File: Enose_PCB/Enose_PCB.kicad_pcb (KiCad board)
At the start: 2 copper layers, 120 x 100 mm, 147 parts, among them IC1 ISL91127IRNZ-T7A, IC2 MP2722GRH-0000-Z, IC3 TPS22958DGNR, J1 Conn_01x04_Pin, J10 Fan, J2 Conn_01x04_Pin, J3 Conn_01x04_Pin, J4 DA15_Pins, J5 USB_C_Receptacle_USB2.0_16P, J6 Battery Terminal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

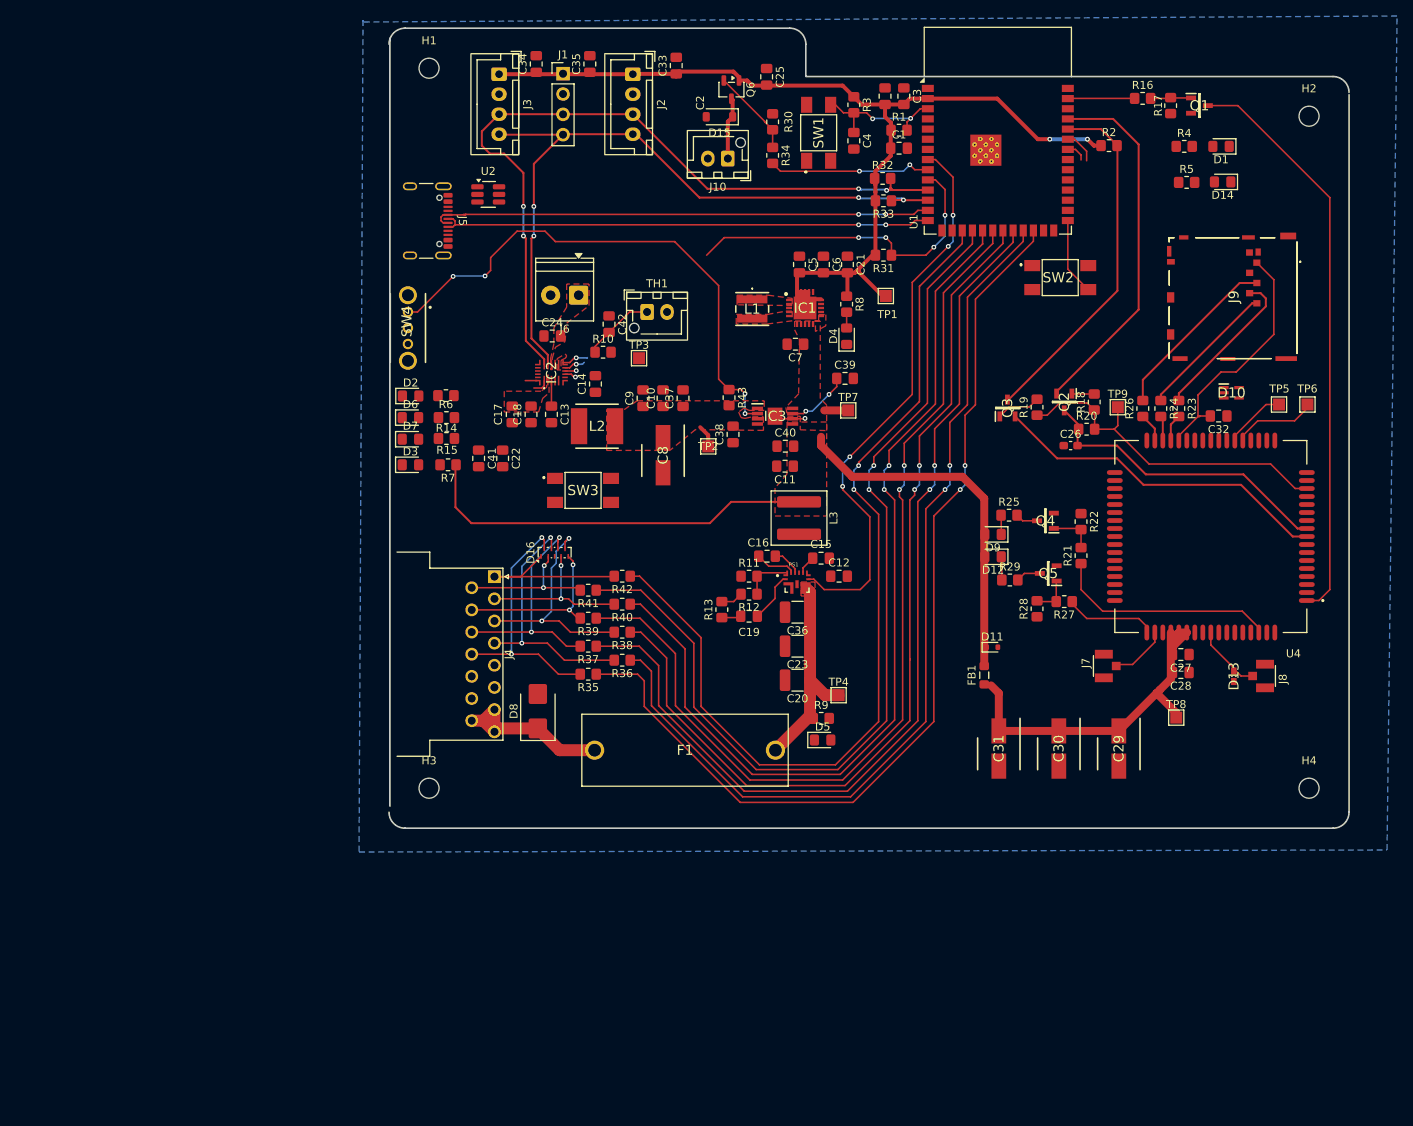
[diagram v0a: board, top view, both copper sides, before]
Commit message: Enose PCB almost done, just needs ground vias
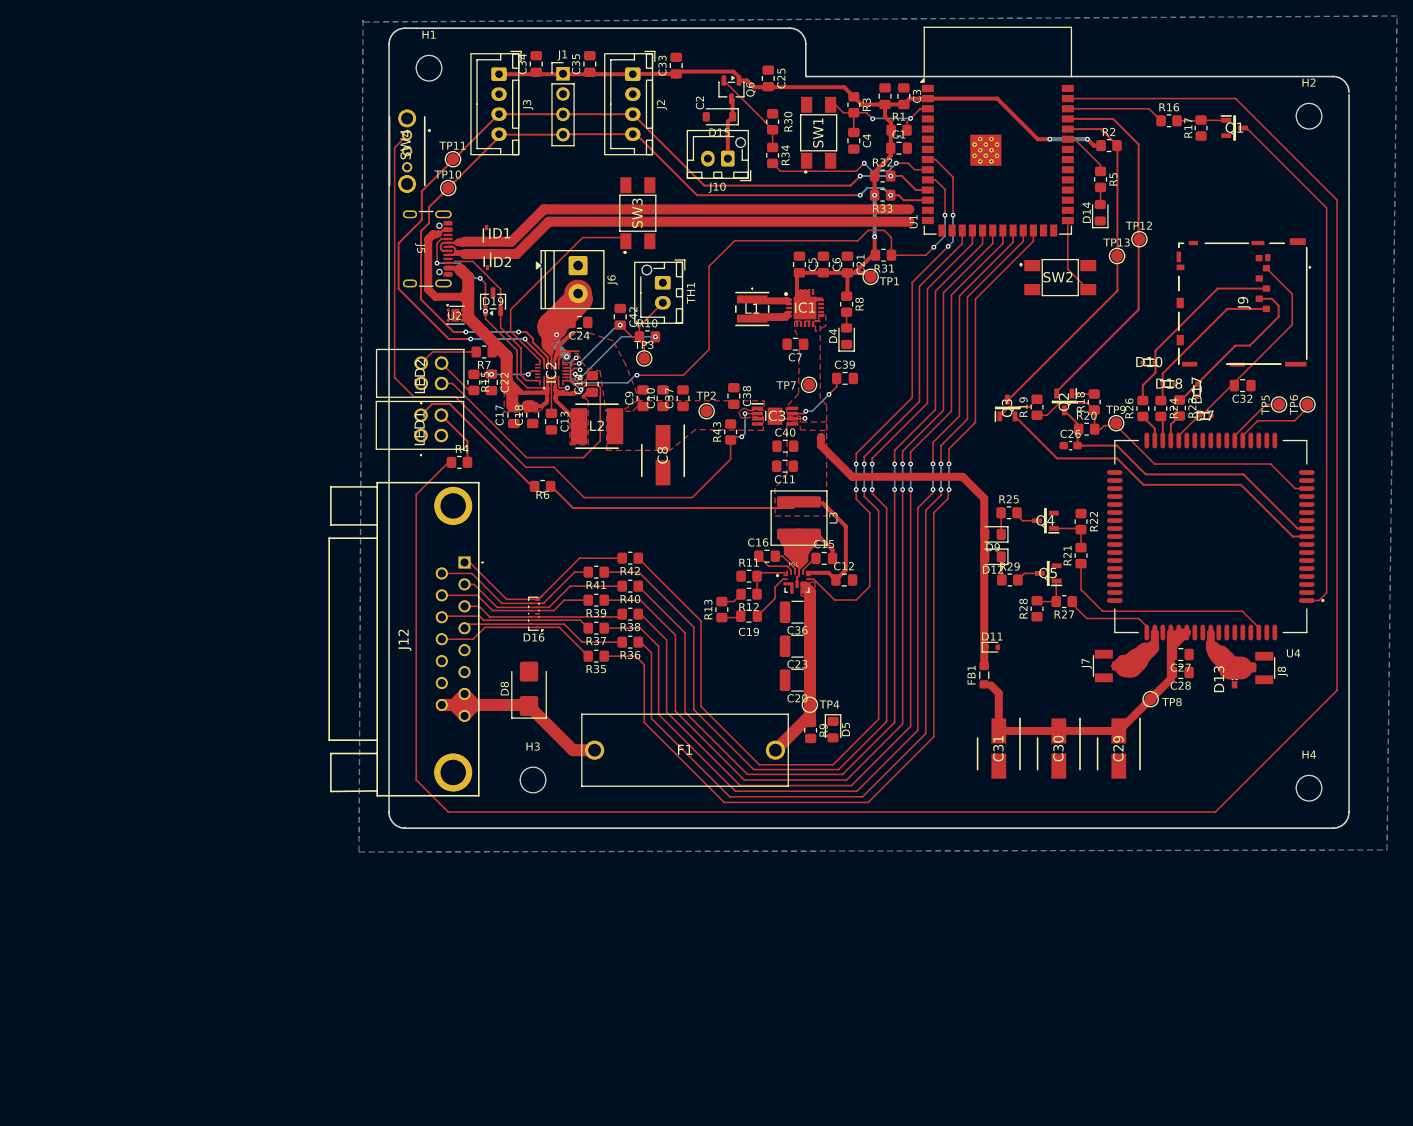
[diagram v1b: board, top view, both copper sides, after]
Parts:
- removed C41: 2.2uF, Capacitor_SMD:C_0805_2012Metric_Pad1.18x1.45mm_HandSolder
- removed D3: LED, LED_SMD:LED_0805_2012Metric_Pad1.15x1.40mm_HandSolder
- removed D6: Amber LED, LED_SMD:LED_0805_2012Metric_Pad1.15x1.40mm_HandSolder
- removed J4: DA15_Pins, Connector_Dsub:DSUB-15_Pins_Horizontal_P2.77x2.84mm_EdgePinOffset9.40mm
- removed R14: 510, Resistor_SMD:R_0805_2012Metric_Pad1.20x1.40mm_HandSolder
- added D17: ESD8351XV2T1G, SamacSys_Parts:SODFL1608X70N, F.Cu at (176.0, 95.3)
- added D18: ESD8351XV2T1G, SamacSys_Parts:SODFL1608X70N, F.Cu at (172.5, 94.5)
- added D19: ESDS452DBZR, Package_TO_SOT_SMD:SOT-23-3, F.Cu at (88.0, 84.2)
- added J12: DA15_Pins_MountingHoles, SamacSys_Parts:6E17C015PAJ121, F.Cu at (84.4, 116.8)
- added LED1: 552-0212F, SamacSys_Parts:5520212F, F.Cu at (79.0, 100.9)
- added LED2: 552-0212F, SamacSys_Parts:5520212F, F.Cu at (79.0, 94.4)
- added TP10: TestPoint, TestPoint:TestPoint_Pad_D1.5mm, F.Cu at (82.4, 70.0)
- added TP11: TestPoint, TestPoint:TestPoint_Pad_D1.5mm, F.Cu at (83.0, 66.4)
- added TP12: TestPoint, TestPoint:TestPoint_Pad_D1.5mm, F.Cu at (168.8, 76.4)
- added TP13: TestPoint, TestPoint:TestPoint_Pad_D1.5mm, F.Cu at (166.0, 78.5)
- D1: value LED Amber -> ESD8351XV2T1G; footprint LED_SMD:LED_0805_2012Metric_Pad1.15x1.40mm_HandSolder -> SamacSys_Parts:SODFL1608X70N
- D10: value ESDALC6V1W5 -> ESD8351XV2T1G; footprint ESDALC6V1W5:SOT65P210X110-5N -> SamacSys_Parts:SODFL1608X70N
- D2: value LED -> ESD8351XV2T1G; footprint LED_SMD:LED_0805_2012Metric_Pad1.15x1.40mm_HandSolder -> SamacSys_Parts:SODFL1608X70N
- D7: value Amber LED -> ESD8351XV2T1G; footprint LED_SMD:LED_0805_2012Metric_Pad1.15x1.40mm_HandSolder -> SamacSys_Parts:SODFL1608X70N
- H1, H2, H3, H4: footprint MountingHole:MountingHole_2.5mm -> MountingHole:MountingHole_3.2mm_M3
- R6: value 1k -> 680
- R7: value 680 -> 1k
- TP1, TP2, TP3, TP4, TP5, TP6, TP7, TP8, TP9: footprint TestPoint:TestPoint_Pad_1.5x1.5mm -> TestPoint:TestPoint_Pad_D1.5mm
- U2: value USBLC6-4SC6 -> TVS0500DRV; footprint Package_TO_SOT_SMD:SOT-23-6_Handsoldering -> Package_SON:WSON-6-1EP_2x2mm_P0.65mm_EP1x1.6mm
- moved D7 99.4 mm to (177.0, 98.5)
- moved R4 98.8 mm to (83.8, 104.3)
- moved D1 92.4 mm to (87.2, 75.7), turned to 90 degrees
- moved SW3 35.3 mm to (106.1, 73.2), turned to 90 degrees
- moved SW4 22.1 mm to (77.3, 65.4)
- moved D2 19.3 mm to (87.3, 79.2), turned to -90 degrees
- moved R6 16.6 mm to (94.2, 107.3)
- moved D14 15.8 mm to (163.9, 73.1), turned to 90 degrees
- moved U2 15.6 mm to (83.3, 85.9)
- moved R7 14.8 mm to (86.9, 90.5)
- moved H3 13.0 mm to (93.0, 144.0)
- moved D10 11.0 mm to (170.0, 91.8), turned to 180 degrees
- moved R5 10.8 mm to (163.9, 68.9), turned to -90 degrees
- moved C22 9.60 mm to (87.8, 94.3)
- moved D16 8.08 mm to (93.1, 123.2), turned to 180 degrees
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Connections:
- net /ESP_LED2 renamed Net-(U1-IO42)
- net Net-(IC2-SW) renamed /Power Components/SW_Inductor_IN
- D1 pad 1: GND -> USB_D-
- D1 pad 2: Net-(D1-A) -> GND
- D10 pad 1: Net-(J9-I/O) -> Net-(D10-K)
- D2 pad 1: GND -> USB_D+
- D2 pad 2: Net-(D2-A) -> GND
- D7 pad 1: /Power Components/STAT/IB -> /Cellular Module/SIM_VDD
- D7 pad 2: Net-(D7-A) -> GND
- J6 pad 1: +BATT -> GND
- J6 pad 2: GND -> +BATT
- J9 pad 2: Net-(J9-RST) -> Net-(D10-K)
- J9 pad 3: Net-(J9-CLK) -> Net-(D18-K)
- J9 pad 6: Net-(J9-I/O) -> Net-(D17-K)
- R15 pad 2: Net-(D7-A) -> Net-(LED2-ANODE_2)
- R23 pad 1: Net-(J9-I/O) -> Net-(D17-K)
- R24 pad 1: Net-(J9-CLK) -> Net-(D18-K)
- R26 pad 2: Net-(J9-RST) -> Net-(D10-K)
- R35 pad 1: /PWM8 -> /PWM1
- R35 pad 2: Net-(D16-K8) -> Net-(D16-K1)
- R36 pad 1: /PWM7 -> /PWM2
- R36 pad 2: Net-(D16-K7) -> Net-(D16-K8)
- R37 pad 1: /PWM6 -> /PWM3
- R37 pad 2: Net-(D16-K6) -> Net-(D16-K2)
- R38 pad 1: /PWM5 -> /PWM4
- R38 pad 2: Net-(D16-K5) -> Net-(D16-K7)
- R39 pad 1: /PWM4 -> /PWM5
- R39 pad 2: Net-(D16-K4) -> Net-(D16-K6)
- R4 pad 1: /ESP_LED1 -> /POWER_STATUS
- R4 pad 2: Net-(D1-A) -> Net-(LED1-ANODE_2)
- R40 pad 1: /PWM3 -> /PWM6
- R41 pad 1: /PWM2 -> /PWM7
- R41 pad 2: Net-(D16-K2) -> Net-(D16-K5)
- R42 pad 1: /PWM1 -> /PWM8
- R42 pad 2: Net-(D16-K1) -> Net-(D16-K4)
- R6 pad 1: VBUS -> +SYS_SW
- R6 pad 2: Net-(D2-A) -> Net-(LED1-ANODE_1)
- R7 pad 1: +SYS_SW -> +VBUS
- TH1 pad 1: /Power Components/NTC1 -> GND
- TH1 pad 2: GND -> /Power Components/NTC1
- U1 pad 17: /PWM1 -> /PWM8
- U1 pad 18: /PWM2 -> /PWM7
- U1 pad 19: /PWM3 -> /PWM6
- U1 pad 20: /PWM4 -> /PWM5
- U1 pad 21: /PWM5 -> /PWM4
- U1 pad 22: /PWM6 -> /PWM3
- U1 pad 23: /PWM7 -> /PWM2
- U1 pad 24: /PWM8 -> /PWM1
- U1 pad 34: /ESP_LED1 -> unconnected-(U1-IO41-Pad34)
- U1 pad 38: unconnected-(U1-IO2-Pad38) -> PWRKEY
- U1 pad 39: PWRKEY -> /POWER_STATUS
- U2 pad 1: /Power Components/CC1 -> GND
- U2 pad 3: /Power Components/CC2 -> GND
- U2 pad 4: USB_D- -> +VBUS
- U2 pad 6: USB_D+ -> +VBUS
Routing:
- net /POWER_STATUS: track 0.00 -> 265.0 mm
- net +VBUS: track 0.00 -> 56.3 mm
- net /Power Components/STAT/IB: track 3.44 -> 40.8 mm, vias 1 -> 2
- net +BATT: track 0.00 -> 31.9 mm, vias 0 -> 2
- net ~{INT}: track 43.4 -> 74.4 mm, vias 5 -> 4
- net Net-(C15-Pad1): track 0.00 -> 27.4 mm
- net /Power Components/CC1: track 2.05 -> 29.4 mm, vias 0 -> 3
- net /Power Components/~{RST}: track 0.00 -> 26.3 mm
- net Net-(D10-K): track 0.00 -> 24.7 mm
- net Net-(IC3-ON): track 66.6 -> 89.7 mm, vias 4 -> 2
- net Net-(J9-RST): track 21.9 -> 0.00 mm
- net Net-(D17-K): track 0.00 -> 20.9 mm
- net /Cellular Module/GNSS_ANT: track 7.07 -> 27.9 mm
- net /Power Components/CC2: track 1.47 -> 22.2 mm
- net Net-(D18-K): track 0.00 -> 19.9 mm
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- added copper zone on F.Cu, net /Power Components/SW_Inductor_IN
- removed copper zone on F.Cu, net +BATT
- removed copper zone on F.Cu, net /Power Components/LX1
- removed copper zone on F.Cu, net /Power Components/LX2
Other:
- outline, holes or cut-outs redrawn

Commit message: Enose board ready for review
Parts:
- added H5: MountingHole, MountingHole:MountingHole_3.2mm_M3, F.Cu at (53.7, 146.4)
- added J4: Conn_01x05_Pin, Connector_PinHeader_2.54mm:PinHeader_1x05_P2.54mm_Vertical, F.Cu at (126.2, 102.3)
- added TP14: TestPoint, TestPoint:TestPoint_Pad_D1.5mm, F.Cu at (133.6, 117.7)
- added TP15: TestPoint, TestPoint:TestPoint_Pad_D1.5mm, F.Cu at (97.3, 121.4)
- added TP16: TestPoint, TestPoint:TestPoint_Pad_D1.5mm, F.Cu at (115.9, 165.1)
- moved D14 70.3 mm to (113.1, 121.7)
- moved R5 70.3 mm to (113.2, 117.5)
- moved TP3 66.4 mm to (51.2, 127.4)
- moved C32 53.2 mm to (141.2, 129.2), turned to -90 degrees
- moved SW2 53.1 mm to (118.2, 115.3), turned to 90 degrees
- moved TP6 52.1 mm to (150.0, 130.8)
- moved R10 52.1 mm to (67.2, 121.8), turned to -90 degrees
- moved TP11 51.5 mm to (43.4, 99.4)
- moved C42 51.3 mm to (65.0, 119.5)
- moved Q1 51.0 mm to (143.2, 97.0)
- moved R16 51.0 mm to (135.1, 96.2)
- moved R17 51.0 mm to (139.1, 97.0)
- moved C36 50.9 mm to (87.0, 155.8)
- moved TP10 50.9 mm to (43.2, 102.4)
- moved H3 50.8 mm to (53.7, 176.2)
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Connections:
- R5 pad 1: Net-(U1-IO42) -> Net-(U1-IO38)
- TP3 pad 1: /Power Components/NTC1 -> +VBUS
- U1 pad 31: unconnected-(U1-IO38-Pad31) -> Net-(U1-IO38)
- U1 pad 33: unconnected-(U1-IO40-Pad33) -> Net-(J4-Pin_5)
- U1 pad 34: unconnected-(U1-IO41-Pad34) -> Net-(J4-Pin_4)
- U1 pad 35: Net-(U1-IO42) -> Net-(J4-Pin_3)
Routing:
- net Net-(U1-IO38): track 0.00 -> 22.6 mm
- net Net-(J4-Pin_5): track 0.00 -> 16.5 mm
- net Net-(J4-Pin_4): track 0.00 -> 15.2 mm
- net Net-(J4-Pin_3): track 0.00 -> 14.0 mm
- net +15V: track 22.1 -> 32.3 mm
- net GND: track 11.8 -> 20.1 mm, vias 2 -> 422
- net USB_D+: track 64.3 -> 71.8 mm
- net Net-(U1-IO42): track 6.21 -> 0.00 mm
- net +3V3: track 132.8 -> 138.2 mm
- net ~{INT}: track 74.4 -> 69.2 mm
- net USB_D-: track 65.3 -> 69.5 mm
- net /Power Components/NTC1: track 20.5 -> 16.9 mm
- net Net-(SW2-B): track 9.69 -> 6.46 mm
- net Net-(D5-A): track 0.00 -> 2.91 mm
- net Net-(D17-K): track 20.9 -> 23.7 mm
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- added copper zone on F.Cu, net GND
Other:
- outline, holes or cut-outs redrawn
- board text added: "15V"
- board text added: "3V3"
- board text added: "GND"
- board text added: "GPIO40"
- board text added: "GPIO41"
- board text added: "GPIO42"
- board text added: "NTC"
- board text added: "RX"
- board text added: "RXD"
- board text added: "SCL"
- board text added: "SDA"
- board text added: "SYS"
- board text added: "SYS_SW"
- board text added: "TX"
- board text added: "TXD"
- board text added: "VBAT"
- board text added: "VBUS"
- board text added: "VDD_EXT"
- board text added: "VFAN"
- board text added: "Vin"

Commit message: Enose PCB finished
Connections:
- IC2 pad 9: /Power Components/PG/NTC2 -> unconnected-(IC2-PG/_NTC2-Pad9)
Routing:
- net +BATT: track 31.9 -> 27.6 mm
- net I2C_SDA: track 109.0 -> 109.5 mm
- net GND: vias 422 -> 421
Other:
- board text added: "BOOT"
- board text added: "MP2722 RESTART"
- board text added: "RESTART"
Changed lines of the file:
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@@
 	(net 18 "Net-(D4-A)")
 	(net 19 "Net-(D5-A)")
-	(net 20 "/Power Components/PG{slash}NTC2")
+	(net 20 "unconnected-(IC2-PG{slash}_NTC2-Pad9)")
 	(net 21 "/POWER_STATUS")
 	(net 22 "/Power Components/STAT{slash}IB")
@@
 		(tags "Integrated Circuit")
 		(property "Reference" "IC2"
-			(at 3.525 0.15 180)
+			(at 3.525 -0.05 180)
 			(layer "F.SilkS")
 			(effects
@@
 			(size 0.2 0.7)
 			(layers "F.Cu" "F.Mask" "F.Paste")
-			(net 20 "/Power Components/PG{slash}NTC2")
+			(net 20 "unconnected-(IC2-PG{slash}_NTC2-Pad9)")
 			(pinfunction "PG/_NTC2")
-			(pintype "passive")
+			(pintype "passive+no_connect")
 		)
 		(pad "10" smd rect
@@
 			(at 0.05 3.95 270)
 			(layer "F.SilkS")
+			(hide yes)
 			(effects
 				(font
@@
 			(at -6.75 0.05 180)
 			(layer "F.SilkS")
+			(hide yes)
 			(effects
 				(font
@@
 			(at 0 4.95 180)
 			(layer "F.SilkS")
+			(hide yes)
 			(effects
 				(font
@@
 		)
 	)
+	(gr_text "MP2722\nRESTART"
+		(at 63.8 106 0)
+		(layer "F.SilkS")
+		(effects
+			(font
+				(size 1 1)
+				(thickness 0.2)
+				(bold yes)
+			)
+			(justify right bottom)
+		)
+	)
 	(gr_text "RX"
 		(at 131.2 100.4 0)
@@
 		)
 	)
+	(gr_text "RESTART"
+		(at 86.6 102.6 0)
+		(layer "F.SilkS")
+		(effects
+			(font
+				(size 1 1)
+				(thickness 0.2)
+				(bold yes)
+			)
+			(justify left bottom)
+		)
+	)
 	(gr_text "Vin"
 		(at 132.7 166.7 0)
@@
 		)
 	)
+	(gr_text "BOOT"
+		(at 122.6 117.6 90)
+		(layer "F.SilkS")
+		(effects
+			(font
+				(size 1 1)
+				(thickness 0.2)
+				(bold yes)
+			)
+			(justify left bottom)
+		)
+	)
 	(gr_text "GND"
 		(at 98.6 122 0)
@@
 	)
 	(via
-		(at 49.975 112.775)
+		(at 49.6 112.5)
 		(size 0.6)
 		(drill 0.3)
@@
 	)
 	(via
-		(at 38.225 120.225)
+		(at 38.2 119.9)
 		(size 0.6)
 		(drill 0.3)
@@
 	)
 	(via
-		(at 48.25 112.2)
-		(size 0.6)
-		(drill 0.3)
-		(layers "F.Cu" "B.Cu")
-		(net 1)
-	)
-	(via
 		(at 43 95.8)
 		(size 0.6)
@@
 	)
 	(segment
-		(start 56.894135 120.594135)
-		(end 56.25 121.23827)
-		(width 0.5)
-		(layer "F.Cu")
-		(net 4)
-	)
-	(segment
 		(start 57.15 123.674)
 		(end 57.474 123.35)
@@
 	)
 	(segment
-		(start 55.85 121.15)
-		(end 57.342127 119.657873)
-		(width 0.5)
-		(layer "F.Cu")
-		(net 4)
-	)
-	(segment
 		(start 56.342127 119.657873)
 		(end 57.3875 119.657873)
@@
 	)
 	(segment
-		(start 56.894135 120.594135)
-		(end 56.33827 121.15)
-		(width 0.5)
-		(layer "F.Cu")
-		(net 4)
-	)
-	(segment
 		(start 56.25 122.735412)
 		(end 56.25 121.75)
@@
 	)
 	(segment
-		(start 56.33827 121.15)
-		(end 56.25 121.15)
-		(width 0.5)
-		(layer "F.Cu")
-		(net 4)
-	)
-	(segment
 		(start 55.407294 122.192706)
 		(end 56.15 122.935412)
@@
 	)
 	(via
-		(at 56.894135 120.594135)
+		(at 56 121.6)
 		(size 0.6)
 		(drill 0.3)
@@
 	)
 	(segment
-		(start 56.894135 120.594135)
-		(end 56.894135 121.994135)
-		(width 1)
-		(layer "B.Cu")
-		(net 4)
-	)
-	(segment
-		(start 58.15 123.25)
-		(end 58.15 123.35)
-		(width 1)
+		(start 58.15 123.35)
+		(end 57.75 123.35)
+		(width 0.5)
 		(layer "B.Cu")
 		(net 4)
 	)
 	(segment
-		(start 56.894135 121.994135)
-		(end 58.15 123.25)
-		(width 1)
+		(start 57.75 123.35)
+		(end 56 121.6)
+		(width 0.5)
 		(layer "B.Cu")
 		(net 4)
@@
 	)
 	(segment
-		(start 52.974265 121.125735)
-		(end 52.974265 121.274265)
+		(start 55.35 124.325)
+		(end 55.35 123.65)
 		(width 0.25)
 		(layer "F.Cu")
@@
 	(segment
 		(start 55.35 123.65)
-		(end 55.35 124.325)
+		(end 52.3258 120.6258)
 		(width 0.25)
 		(layer "F.Cu")
@@
 	)
 	(segment
-		(start 94.5 101.1)
-		(end 74.5 101.1)
+		(start 52.3258 120.6258)
+		(end 52.3258 120.477273)
 		(width 0.25)
 		(layer "F.Cu")
@@
 	)
 	(segment
-		(start 52.974265 121.274265)
-		(end 55.35 123.65)
+		(start 94.5 101.1)
+		(end 74.5 101.1)
 		(width 0.25)
 		(layer "F.Cu")
@@
 	)
 	(via
-		(at 52.974265 121.125735)
+		(at 52.3258 120.477273)
 		(size 0.6)
 		(drill 0.3)
@@
 	)
 	(segment
-		(start 52.974265 121.125735)
+		(start 52.3258 120.477273)
+		(end 51.677338 121.125735)
+		(width 0.25)
+		(layer "B.Cu")
+		(net 40)
+	)
+	(segment
+		(start 51.677338 121.125735)
 		(end 46.15 121.125735)
 		(width 0.25)
@@
 	)
 	(segment
-		(start 44.169 111.431)
-		(end 46.431 111.431)
+		(start 49.9 114.9)
+		(end 49.9 117.5875)
 		(width 0.2)
 		(layer "F.Cu")
@@
 	)
 	(segment
+		(start 44.169 111.431)
+		(end 46.431 111.431)
+		(width 0.2)
+		(layer "F.Cu")
+		(net 42)
+	)
+	(segment
 		(start 52.45 122.25)
 		(end 49.9 119.7)
@@
 	)
 	(segment
-		(start 49.9 114.9)
-		(end 49.9 117.5875)
+		(start 46.431 111.431)
+		(end 49.9 114.9)
 		(width 0.2)
 		(layer "F.Cu")
@@
 	)
 	(segment
-		(start 46.431 111.431)
-		(end 49.9 114.9)
-		(width 0.2)
-		(layer "F.Cu")
-		(net 42)
-	)
-	(segment
 		(start 59.856275 126.017635)
 		(end 59.52391 126.35)
@@
 	)
 	(segment
+		(start 55.8 123.4)
+		(end 55.8 124.325)
+		(width 0.25)
+		(layer "F.Cu")
+		(net 45)
+	)
+	(segment
 		(start 94.85 103.15)
 		(end 93.725 102.025)
@@
 	)
 	(segment
-		(start 53.95 121.55)
-		(end 55.8 123.4)
+		(start 53.95 121.1)
+		(end 53.95 121.55)
 		(width 0.25)
 		(layer "F.Cu")
@@
 	)
 	(segment
-		(start 55.8 123.4)
-		(end 55.8 124.325)
-		(width 0.25)
-		(layer "F.Cu")
-		(net 45)
-	)
-	(segment
 		(start 49.76 95.585)
 		(end 49.7 95.525)
@@
 	)
 	(segment
+		(start 51.9 119.8)
+		(end 52.65 119.8)
+		(width 0.25)
+		(layer "F.Cu")
+		(net 45)
+	)
+	(segment
 		(start 42.15 120.25)
 		(end 39.95 118.05)
@@
 	)
 	(segment
-		(start 102.475 103.775)
-		(end 103.3 103.775)
+		(start 52.65 119.8)
+		(end 53.95 121.1)
 		(width 0.25)
 		(layer "F.Cu")
@@
 	)
 	(segment
-		(start 53.1 120.25)
-		(end 52.15 120.25)
+		(start 102.475 103.775)
+		(end 103.3 103.775)
 		(width 0.25)
 		(layer "F.Cu")
@@
 	)
 	(segment
-		(start 53.95 121.1)
-		(end 53.95 121.55)
+		(start 53.95 121.55)
+		(end 55.8 123.4)
 		(width 0.25)
 		(layer "F.Cu")
@@
 		(net 45)
 	)
-	(segment
-		(start 53.95 121.1)
-		(end 53.1 120.25)
-		(width 0.25)
-		(layer "F.Cu")
-		(net 45)
-	)
 	(via
 		(at 94.85 103.15)
@@
 	)
 	(via
-		(at 52.15 120.25)
+		(at 51.9 119.8)
 		(size 0.6)
 		(drill 0.3)
@@
 	)
 	(segment
+		(start 45.55 120.25)
+		(end 51.45 120.25)
+		(width 0.25)
+		(layer "B.Cu")
+		(net 45)
+	)
+	(segment
 		(start 97.85 102.35)
 		(end 98.65 103.15)
@@
 	)
 	(segment
-		(start 95.65 102.35)
-		(end 97.85 102.35)
+		(start 51.45 120.25)
+		(end 51.9 119.8)
 		(width 0.25)
 		(layer "B.Cu")
@@
 	)
 	(segment
-		(start 45.55 120.25)
-		(end 52.15 120.25)
+		(start 95.65 102.35)
+		(end 97.85 102.35)
 		(width 0.25)
 		(layer "B.Cu")
